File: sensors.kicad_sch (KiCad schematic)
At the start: 24 parts, among them J10 PH-2P, J11 PH-2P, J12 PH-2P, J13 PH-2P, J14 PH-2P, J15 PH-3P

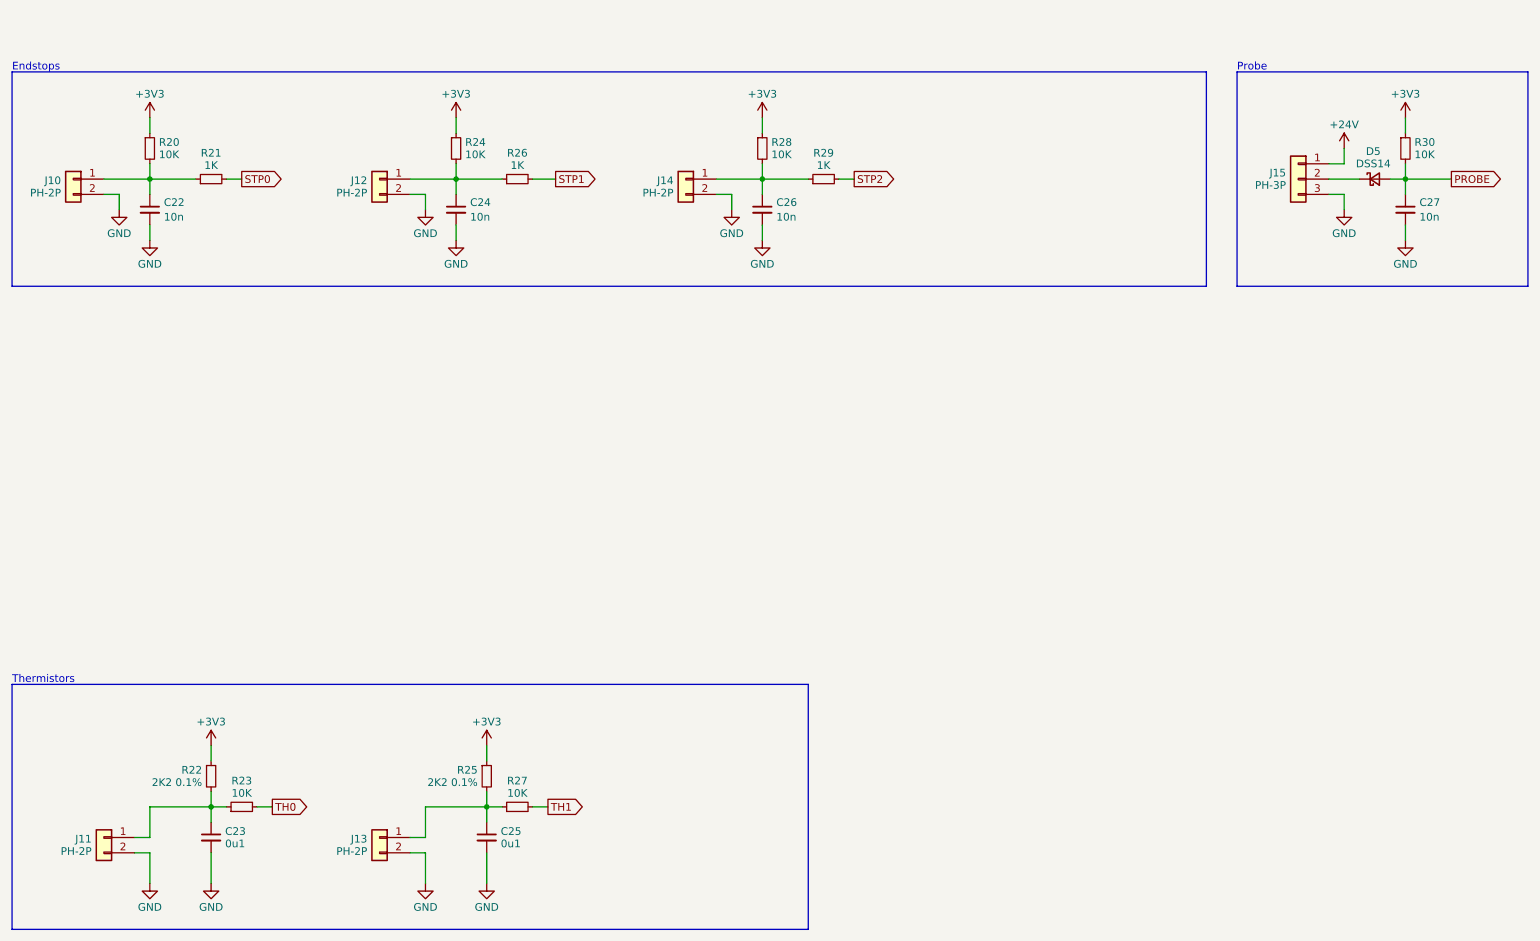
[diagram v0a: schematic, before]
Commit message: Added solder jumpers for CAN/USB interface selection
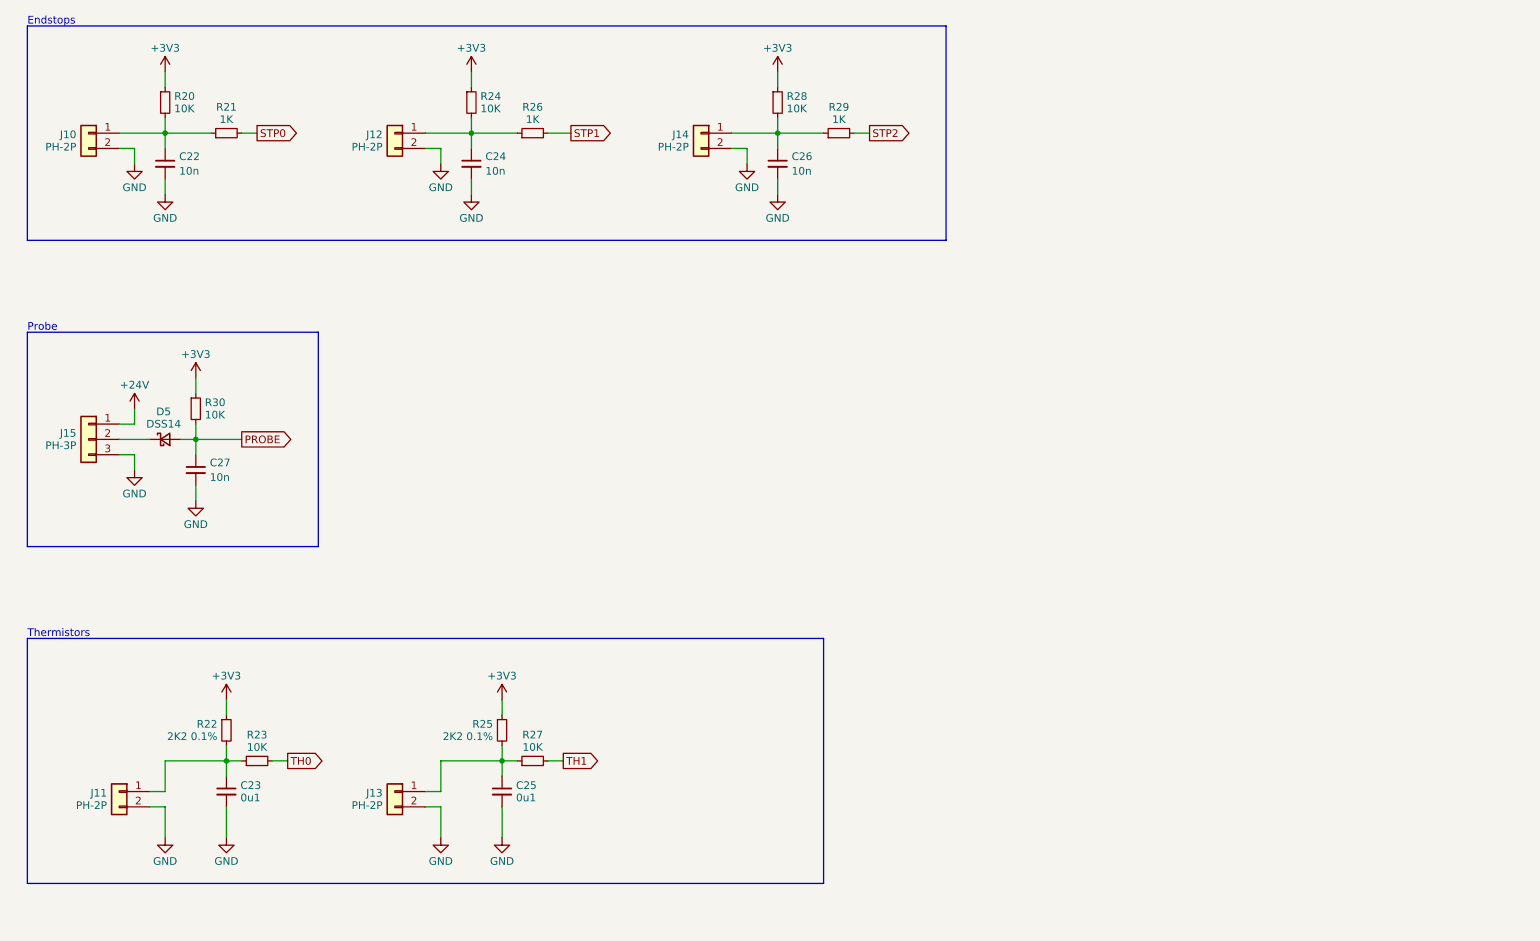
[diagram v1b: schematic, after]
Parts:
- R22, R25: LCSC (none) -> C326602
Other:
- moved on the sheet: C22, C23, C24, C25, C26, C27, D5, J10, J11, J12, J13, J14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

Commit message: Add part number references
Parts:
- C22, C24, C26, C27: manf# (none) -> CL05B103KB5NNNC
- C23, C25: manf# (none) -> GRM155R71H104KE14J
- D5: digikey# (none) -> 1655-DSS14UCT-ND; manf# (none) -> DSS14
- J10, J11, J12, J13, J14: manf# (none) -> B2B-PH-K-S
- J15: manf# (none) -> B3B-PH-K-S
- R20, R23, R24, R27, R28, R30: manf# (none) -> RMCF0402FT10K0
- R21, R26, R29: manf# (none) -> RMCF0402JT1K00
- R22, R25: manf# (none) -> RNCF0402BTE2K20

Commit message: Change input caps
- 100uF to electrolytic
- 10uF to 1206/50V
- Also fix LED on BOM to not be right angle lol
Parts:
- D5: MPN DSS14 -> (none)
- R22, R25: manf# RNCF0402BTE2K20 -> RT0402BRE072K2L
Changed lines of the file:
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@@
 			)
 		)
-		(property "MPN" ""
-			(at 48.26 38.1 0)
-			(effects
-				(font
-					(size 1.27 1.27)
-				)
-				(hide yes)
-			)
-		)
 		(property "LCSC" "C25744"
 			(at 48.26 38.1 0)
@@
 			)
 		)
-		(property "MPN" ""
-			(at 109.22 43.18 0)
-			(effects
-				(font
-					(size 1.27 1.27)
-				)
-				(hide yes)
-			)
-		)
 		(property "LCSC" "C11702"
 			(at 109.22 43.18 0)
@@
 			)
 		)
-		(property "MPN" ""
-			(at 99.06 38.1 0)
-			(effects
-				(font
-					(size 1.27 1.27)
-				)
-				(hide yes)
-			)
-		)
 		(property "LCSC" "C25744"
 			(at 99.06 38.1 0)
@@
 			)
 		)
-		(property "MPN" ""
-			(at 86.36 43.18 0)
-			(effects
-				(font
-					(size 1.27 1.27)
-				)
-				(hide yes)
-			)
-		)
 		(property "LCSC" "C131337"
 			(at 86.36 43.18 0)
@@
 			)
 		)
-		(property "MPN" ""
-			(at 63.5 147.32 0)
-			(effects
-				(font
-					(size 1.27 1.27)
-				)
-				(hide yes)
-			)
-		)
 		(property "LCSC" "C25744"
 			(at 63.5 147.32 0)
@@
 			)
 		)
-		(property "MPN" ""
-			(at 149.86 38.1 0)
-			(effects
-				(font
-					(size 1.27 1.27)
-				)
-				(hide yes)
-			)
-		)
 		(property "LCSC" "C25744"
 			(at 149.86 38.1 0)
@@
 			)
 		)
-		(property "MPN" ""
-			(at 58.42 43.18 0)
-			(effects
-				(font
-					(size 1.27 1.27)
-				)
-				(hide yes)
-			)
-		)
 		(property "LCSC" "C11702"
 			(at 58.42 43.18 0)
@@
 			)
 		)
-		(property "MPN" ""
-			(at 40.64 152.4 0)
-			(effects
-				(font
-					(size 1.27 1.27)
-				)
-				(hide yes)
-			)
-		)
 		(property "LCSC" "C131337"
 			(at 40.64 152.4 0)
@@
 			)
 		)
-		(property "MPN" ""
-			(at 160.02 43.18 0)
-			(effects
-				(font
-					(size 1.27 1.27)
-				)
-				(hide yes)
-			)
-		)
 		(property "LCSC" "C11702"
 			(at 160.02 43.18 0)
@@
 			)
 		)
-		(property "MPN" ""
-			(at 53.34 99.06 0)
-			(effects
-				(font
-					(size 1.27 1.27)
-				)
-				(hide yes)
-			)
-		)
 		(property "LCSC" "C15195"
 			(at 53.34 99.06 0)
@@
 			)
 		)
-		(property "MPN" "DSS14"
-			(at 48.26 93.98 0)
-			(effects
-				(font
-					(size 1.27 1.27)
-				)
-				(hide yes)
-			)
-		)
 		(property "digikey#" "1655-DSS14UCT-ND"
 			(at 48.26 93.98 0)
@@
 			)
 		)
-		(property "MPN" ""
-			(at 149.86 48.26 0)
-			(effects
-				(font
-					(size 1.27 1.27)
-				)
-				(hide yes)
-			)
-		)
 		(property "LCSC" "C15195"
 			(at 149.86 48.26 0)
@@
 			)
 		)
-		(property "MPN" ""
-			(at 58.42 152.4 0)
-			(effects
-				(font
-					(size 1.27 1.27)
-				)
-				(hide yes)
-			)
-		)
 		(property "LCSC" "C307331"
 			(at 58.42 152.4 0)
@@
 			)
 		)
-		(property "MPN" ""
-			(at 109.22 147.32 0)
-			(effects
-				(font
-					(size 1.27 1.27)
-				)
-				(hide yes)
-			)
-		)
 		(property "LCSC" "C25744"
 			(at 109.22 147.32 0)
@@
 			)
 		)
-		(property "MPN" ""
-			(at 104.14 142.24 0)
-			(effects
-				(font
-					(size 1.27 1.27)
-				)
-				(hide yes)
-			)
-		)
 		(property "LCSC" "C326602"
 			(at 104.14 142.24 0)
@@
 			)
 		)
-		(property "manf#" "RNCF0402BTE2K20"
+		(property "manf#" "RT0402BRE072K2L"
 			(at 104.14 142.24 0)
 			(effects
@@
 			)
 		)
-		(property "MPN" ""
-			(at 58.42 142.24 0)
-			(effects
-				(font
-					(size 1.27 1.27)
-				)
-				(hide yes)
-			)
-		)
 		(property "LCSC" "C326602"
 			(at 58.42 142.24 0)
@@
 			)
 		)
-		(property "manf#" "RNCF0402BTE2K20"
+		(property "manf#" "RT0402BRE072K2L"
 			(at 58.42 142.24 0)
 			(effects
@@
 			)
 		)
-		(property "MPN" ""
-			(at 48.26 48.26 0)
-			(effects
-				(font
-					(size 1.27 1.27)
-				)
-				(hide yes)
-			)
-		)
 		(property "LCSC" "C15195"
 			(at 48.26 48.26 0)
@@
 			)
 		)
-		(property "MPN" ""
-			(at 35.56 93.98 0)
-			(effects
-				(font
-					(size 1.27 1.27)
-				)
-				(hide yes)
-			)
-		)
 		(property "LCSC" "C131339"
 			(at 35.56 93.98 0)
@@
 			)
 		)
-		(property "MPN" ""
-			(at 53.34 88.9 0)
-			(effects
-				(font
-					(size 1.27 1.27)
-				)
-				(hide yes)
-			)
-		)
 		(property "LCSC" "C25744"
 			(at 53.34 88.9 0)
@@
 			)
 		)
-		(property "MPN" ""
-			(at 35.56 43.18 0)
-			(effects
-				(font
-					(size 1.27 1.27)
-				)
-				(hide yes)
-			)
-		)
 		(property "LCSC" "C131337"
 			(at 35.56 43.18 0)
@@
 			)
 		)
-		(property "MPN" ""
-			(at 86.36 152.4 0)
-			(effects
-				(font
-					(size 1.27 1.27)
-				)
-				(hide yes)
-			)
-		)
 		(property "LCSC" "C131337"
 			(at 86.36 152.4 0)
@@
 			)
 		)
-		(property "MPN" ""
-			(at 137.16 43.18 0)
-			(effects
-				(font
-					(size 1.27 1.27)
-				)
-				(hide yes)
-			)
-		)
 		(property "LCSC" "C131337"
 			(at 137.16 43.18 0)
@@
 			)
 		)
-		(property "MPN" ""
-			(at 99.06 48.26 0)
-			(effects
-				(font
-					(size 1.27 1.27)
-				)
-				(hide yes)
-			)
-		)
 		(property "LCSC" "C15195"
 			(at 99.06 48.26 0)
@@
 			(at 104.14 152.4 0)
 			(effects
-				(font
-					(size 1.27 1.27)
-				)
-				(hide yes)
-			)
-		)
-		(property "MPN" ""
-			(at 104.14 152.4 0)
-			(effects

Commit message: Change 5V out cap to 0805
- Shifted power/CAN connector a bit to make room, and added a bit of
  meat to the board around the mounting hole
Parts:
- D5: mouser# (none) -> 241-SS1040FLR100001
- R20, R23, R24, R27, R28, R30: manf# RMCF0402FT10K0 -> RC0402FR-0710KL
- R21, R26, R29: manf# RMCF0402JT1K00 -> RC0402FR-071KL
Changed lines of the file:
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@@
 			)
 		)
-		(property "manf#" "RMCF0402FT10K0"
+		(property "manf#" "RC0402FR-0710KL"
+			(at 48.26 38.1 0)
+			(effects
+				(font
+					(size 1.27 1.27)
+				)
+				(hide yes)
+			)
+		)
+		(property "mouser#" ""
 			(at 48.26 38.1 0)
 			(effects
@@
 			)
 		)
-		(property "manf#" "RMCF0402JT1K00"
+		(property "manf#" "RC0402FR-071KL"
+			(at 109.22 43.18 0)
+			(effects
+				(font
+					(size 1.27 1.27)
+				)
+				(hide yes)
+			)
+		)
+		(property "mouser#" ""
 			(at 109.22 43.18 0)
 			(effects
@@
 			)
 		)
-		(property "manf#" "RMCF0402FT10K0"
+		(property "manf#" "RC0402FR-0710KL"
+			(at 99.06 38.1 0)
+			(effects
+				(font
+					(size 1.27 1.27)
+				)
+				(hide yes)
+			)
+		)
+		(property "mouser#" ""
 			(at 99.06 38.1 0)
 			(effects
@@
 			)
 		)
+		(property "mouser#" ""
+			(at 86.36 43.18 0)
+			(effects
+				(font
+					(size 1.27 1.27)
+				)
+				(hide yes)
+			)
+		)
 		(pin "1"
 		)
@@
 			)
 		)
-		(property "manf#" "RMCF0402FT10K0"
+		(property "manf#" "RC0402FR-0710KL"
+			(at 63.5 147.32 0)
+			(effects
+				(font
+					(size 1.27 1.27)
+				)
+				(hide yes)
+			)
+		)
+		(property "mouser#" ""
 			(at 63.5 147.32 0)
 			(effects
@@
 			)
 		)
-		(property "manf#" "RMCF0402FT10K0"
+		(property "manf#" "RC0402FR-0710KL"
+			(at 149.86 38.1 0)
+			(effects
+				(font
+					(size 1.27 1.27)
+				)
+				(hide yes)
+			)
+		)
+		(property "mouser#" ""
 			(at 149.86 38.1 0)
 			(effects
@@
 			)
 		)
-		(property "manf#" "RMCF0402JT1K00"
+		(property "manf#" "RC0402FR-071KL"
+			(at 58.42 43.18 0)
+			(effects
+				(font
+					(size 1.27 1.27)
+				)
+				(hide yes)
+			)
+		)
+		(property "mouser#" ""
 			(at 58.42 43.18 0)
 			(effects
@@
 			)
 		)
+		(property "mouser#" ""
+			(at 40.64 152.4 0)
+			(effects
+				(font
+					(size 1.27 1.27)
+				)
+				(hide yes)
+			)
+		)
 		(pin "1"
 		)
@@
 			)
 		)
-		(property "manf#" "RMCF0402JT1K00"
+		(property "manf#" "RC0402FR-071KL"
+			(at 160.02 43.18 0)
+			(effects
+				(font
+					(size 1.27 1.27)
+				)
+				(hide yes)
+			)
+		)
+		(property "mouser#" ""
 			(at 160.02 43.18 0)
 			(effects
@@
 			)
 		)
+		(property "mouser#" ""
+			(at 53.34 99.06 0)
+			(effects
+				(font
+					(size 1.27 1.27)
+				)
+				(hide yes)
+			)
+		)
 		(pin "1"
 		)
@@
 			)
 		)
+		(property "mouser#" "241-SS1040FLR100001"
+			(at 48.26 93.98 0)
+			(effects
+				(font
+					(size 1.27 1.27)
+				)
+				(hide yes)
+			)
+		)
 		(pin "1"
 		)
@@
 			)
 		)
+		(property "mouser#" ""
+			(at 149.86 48.26 0)
+			(effects
+				(font
+					(size 1.27 1.27)
+				)
+				(hide yes)
+			)
+		)
 		(pin "1"
 		)
@@
 			)
 		)
+		(property "mouser#" ""
+			(at 58.42 152.4 0)
+			(effects
+				(font
+					(size 1.27 1.27)
+				)
+				(hide yes)
+			)
+		)
 		(pin "1"
 		)
@@
 			)
 		)
-		(property "manf#" "RMCF0402FT10K0"
+		(property "manf#" "RC0402FR-0710KL"
+			(at 109.22 147.32 0)
+			(effects
+				(font
+					(size 1.27 1.27)
+				)
+				(hide yes)
+			)
+		)
+		(property "mouser#" ""
 			(at 109.22 147.32 0)
 			(effects
@@
 			)
 		)
+		(property "mouser#" ""
+			(at 104.14 142.24 0)
+			(effects
+				(font
+					(size 1.27 1.27)
+				)
+				(hide yes)
+			)
+		)
 		(pin "1"
 		)
@@
 			)
 		)
+		(property "mouser#" ""
+			(at 58.42 142.24 0)
+			(effects
+				(font
+					(size 1.27 1.27)
+				)
+				(hide yes)
+			)
+		)
 		(pin "1"
 		)
@@
 			)
 		)
+		(property "mouser#" ""
+			(at 48.26 48.26 0)
+			(effects
+				(font
+					(size 1.27 1.27)
+				)
+				(hide yes)
+			)
+		)
 		(pin "1"
 		)
@@
 			)
 		)
+		(property "mouser#" ""
+			(at 35.56 93.98 0)
+			(effects
+				(font
+					(size 1.27 1.27)
+				)
+				(hide yes)
+			)
+		)
 		(pin "1"
 		)
@@
 			)
 		)
-		(property "manf#" "RMCF0402FT10K0"
+		(property "manf#" "RC0402FR-0710KL"
+			(at 53.34 88.9 0)
+			(effects
+				(font
+					(size 1.27 1.27)
+				)
+				(hide yes)
+			)
+		)
+		(property "mouser#" ""
 			(at 53.34 88.9 0)
 			(effects
@@
 			)
 		)
+		(property "mouser#" ""
+			(at 35.56 43.18 0)
+			(effects
+				(font
+					(size 1.27 1.27)
+				)
+				(hide yes)
+			)
+		)
 		(pin "1"
 		)
@@
 			)
 		)
+		(property "mouser#" ""
+			(at 86.36 152.4 0)
+			(effects
+				(font
+					(size 1.27 1.27)
+				)
+				(hide yes)
+			)
+		)
 		(pin "1"
 		)
@@
 			)
 		)
+		(property "mouser#" ""
+			(at 137.16 43.18 0)
+			(effects
+				(font
+					(size 1.27 1.27)
+				)
+				(hide yes)
+			)
+		)
 		(pin "1"
 		)
@@
 			)
 		)
+		(property "mouser#" ""
+			(at 99.06 48.26 0)
+			(effects
+				(font
+					(size 1.27 1.27)
+				)
+				(hide yes)
+			)
+		)
 		(pin "1"
 		)
@@
 			(at 104.14 152.4 0)
 			(effects
+				(font
+					(size 1.27 1.27)
+				)
+				(hide yes)
+			)
+		)
+		(property "mouser#" ""
+			(at 104.14 152.4 0)
+			(effects

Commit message: Remove DNP from stuff where it doesn't belong in the schematic. Also DNP the fan port caps (the BOM ones weren't rated good for 24V anyway), but in any case since I couldn't find 4.7uF/35V/0603 good for 105C, reduce them to 2.2uF. Too bad I didn't make them 0805
Also added note for higher temp STM32, so I think all the components
should be good to 105C, except for the JST connectors...
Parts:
- C23, C25: Notes (none) -> 50V
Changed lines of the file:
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@@
 			)
 		)
+		(property "Notes" ""
+			(at 48.26 38.1 0)
+			(effects
+				(font
+					(size 1.27 1.27)
+				)
+				(hide yes)
+			)
+		)
 		(pin "1"
 		)
@@
 			)
 		)
+		(property "Notes" ""
+			(at 109.22 43.18 0)
+			(effects
+				(font
+					(size 1.27 1.27)
+				)
+				(hide yes)
+			)
+		)
 		(pin "1"
 		)
@@
 			)
 		)
+		(property "Notes" ""
+			(at 99.06 38.1 0)
+			(effects
+				(font
+					(size 1.27 1.27)
+				)
+				(hide yes)
+			)
+		)
 		(pin "1"
 		)
@@
 			)
 		)
+		(property "Notes" ""
+			(at 86.36 43.18 0)
+			(effects
+				(font
+					(size 1.27 1.27)
+				)
+				(hide yes)
+			)
+		)
 		(pin "1"
 		)
@@
 			)
 		)
+		(property "Notes" ""
+			(at 63.5 147.32 0)
+			(effects
+				(font
+					(size 1.27 1.27)
+				)
+				(hide yes)
+			)
+		)
 		(pin "1"
 		)
@@
 			)
 		)
+		(property "Notes" ""
+			(at 149.86 38.1 0)
+			(effects
+				(font
+					(size 1.27 1.27)
+				)
+				(hide yes)
+			)
+		)
 		(pin "1"
 		)
@@
 			)
 		)
+		(property "Notes" ""
+			(at 58.42 43.18 0)
+			(effects
+				(font
+					(size 1.27 1.27)
+				)
+				(hide yes)
+			)
+		)
 		(pin "1"
 		)
@@
 			)
 		)
+		(property "Notes" ""
+			(at 40.64 152.4 0)
+			(effects
+				(font
+					(size 1.27 1.27)
+				)
+				(hide yes)
+			)
+		)
 		(pin "1"
 		)
@@
 			)
 		)
+		(property "Notes" ""
+			(at 160.02 43.18 0)
+			(effects
+				(font
+					(size 1.27 1.27)
+				)
+				(hide yes)
+			)
+		)
 		(pin "1"
 		)
@@
 			)
 		)
+		(property "Notes" ""
+			(at 53.34 99.06 0)
+			(effects
+				(font
+					(size 1.27 1.27)
+				)
+				(hide yes)
+			)
+		)
 		(pin "1"
 		)
@@
 			)
 		)
+		(property "Notes" ""
+			(at 48.26 93.98 0)
+			(effects
+				(font
+					(size 1.27 1.27)
+				)
+				(hide yes)
+			)
+		)
 		(pin "1"
 		)
@@
 			)
 		)
+		(property "Notes" ""
+			(at 149.86 48.26 0)
+			(effects
+				(font
+					(size 1.27 1.27)
+				)
+				(hide yes)
+			)
+		)
 		(pin "1"
 		)
@@
 			)
 		)
+		(property "Notes" "50V"
+			(at 58.42 152.4 0)
+			(effects
+				(font
+					(size 1.27 1.27)
+				)
+				(hide yes)
+			)
+		)
 		(pin "1"
 		)
@@
 			)
 		)
+		(property "Notes" ""
+			(at 109.22 147.32 0)
+			(effects
+				(font
+					(size 1.27 1.27)
+				)
+				(hide yes)
+			)
+		)
 		(pin "1"
 		)
@@
 			)
 		)
+		(property "Notes" ""
+			(at 104.14 142.24 0)
+			(effects
+				(font
+					(size 1.27 1.27)
+				)
+				(hide yes)
+			)
+		)
 		(pin "1"
 		)
@@
 			)
 		)
+		(property "Notes" ""
+			(at 58.42 142.24 0)
+			(effects
+				(font
+					(size 1.27 1.27)
+				)
+				(hide yes)
+			)
+		)
 		(pin "1"
 		)
@@
 			)
 		)
+		(property "Notes" ""
+			(at 48.26 48.26 0)
+			(effects
+				(font
+					(size 1.27 1.27)
+				)
+				(hide yes)
+			)
+		)
 		(pin "1"
 		)
@@
 			)
 		)
+		(property "Notes" ""
+			(at 35.56 93.98 0)
+			(effects
+				(font
+					(size 1.27 1.27)
+				)
+				(hide yes)
+			)
+		)
 		(pin "1"
 		)
@@
 			)
 		)
+		(property "Notes" ""
+			(at 53.34 88.9 0)
+			(effects
+				(font
+					(size 1.27 1.27)
+				)
+				(hide yes)
+			)
+		)
 		(pin "1"
 		)
@@
 			)
 		)
+		(property "Notes" ""
+			(at 35.56 43.18 0)
+			(effects
+				(font
+					(size 1.27 1.27)
+				)
+				(hide yes)
+			)
+		)
 		(pin "1"
 		)
@@
 			)
 		)
+		(property "Notes" ""
+			(at 86.36 152.4 0)
+			(effects
+				(font
+					(size 1.27 1.27)
+				)
+				(hide yes)
+			)
+		)
 		(pin "1"
 		)
@@
 			)
 		)
+		(property "Notes" ""
+			(at 137.16 43.18 0)
+			(effects
+				(font
+					(size 1.27 1.27)
+				)
+				(hide yes)
+			)
+		)
 		(pin "1"
 		)
@@
 			)
 		)
+		(property "Notes" ""
+			(at 99.06 48.26 0)
+			(effects
+				(font
+					(size 1.27 1.27)
+				)
+				(hide yes)
+			)
+		)
 		(pin "1"
 		)
@@
 			(at 104.14 152.4 0)
 			(effects
+				(font
+					(size 1.27 1.27)
+				)
+				(hide yes)
+			)
+		)
+		(property "Notes" "50V"
+			(at 104.14 152.4 0)
+			(effects
